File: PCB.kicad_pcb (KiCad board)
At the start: 4 copper layers, 130.2 x 64.3 mm, 31 parts, among them J1 Conn_ARM_SWD_TagConnect_TC2030, U2 STM32L476RGTx, U3 NT3H2X11, U4 SSD1306

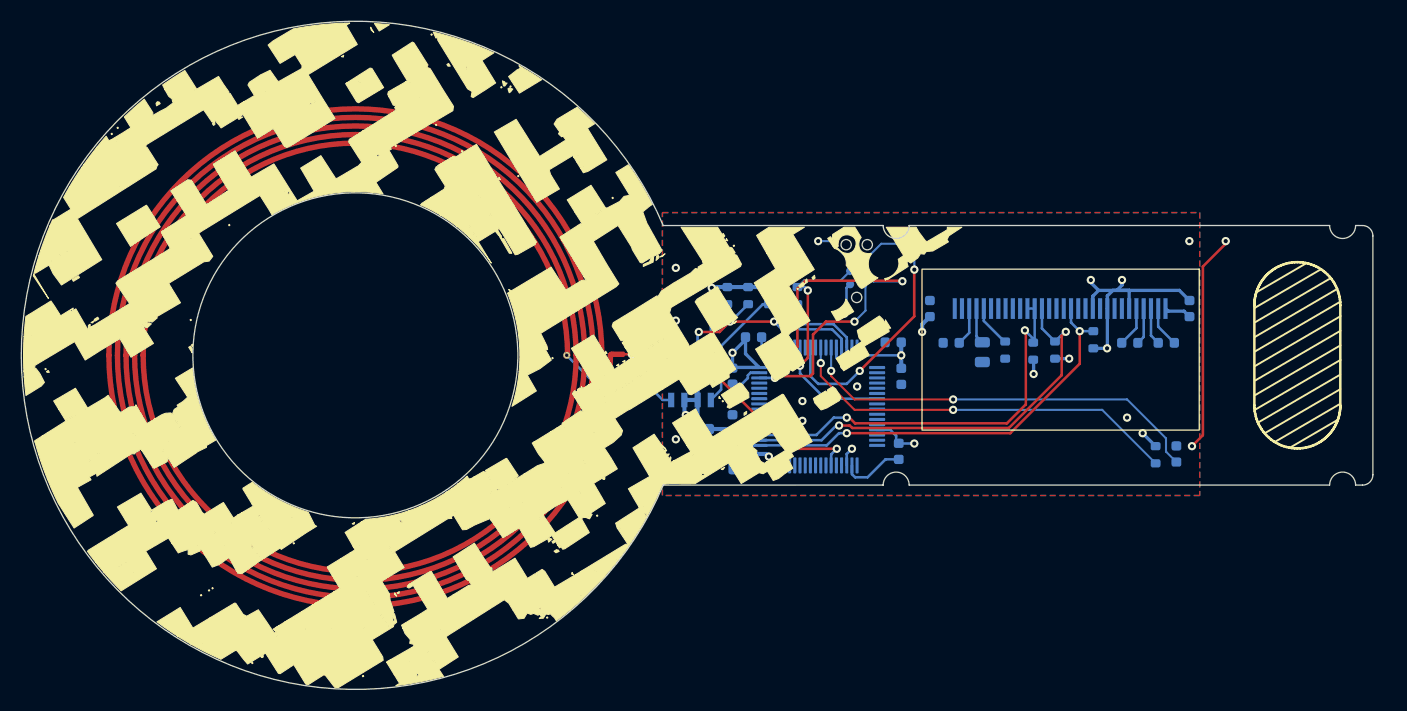
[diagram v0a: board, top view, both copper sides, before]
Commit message: Add board REV-D
Revision D changes the mounting holes so that we can fit screws to
assemble the two case pieces.

Also add required compliance logos on the back.
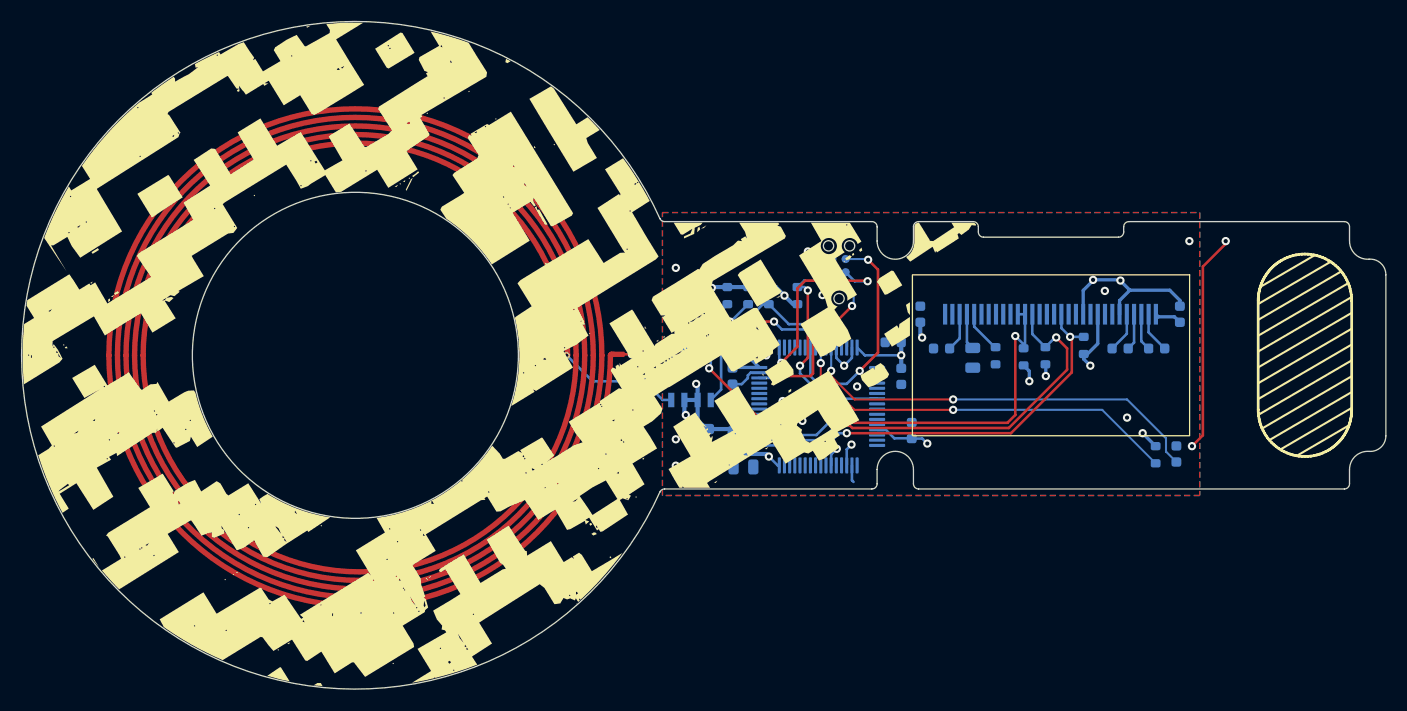
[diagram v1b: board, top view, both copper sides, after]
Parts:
- moved C4 2.36 mm to (136.3, 131.7), turned to 90 degrees
- moved J1 1.70 mm to (129.3, 116.5)
- moved C11 1.07 mm to (142.1, 124.7)
- moved R4 1.07 mm to (152.8, 123.5)
- moved R6 1.07 mm to (149.1, 124.5)
- moved U4 1.07 mm to (149.6, 120.5)
- moved C13 1.07 mm to (159.8, 123.8)
- moved C7 1.07 mm to (139.1, 123.8)
- moved R7 1.07 mm to (147.0, 124.6)
- moved C10 1.07 mm to (162.1, 120.5)
- moved C17 1.07 mm to (137.1, 120.5)
- moved R5 1.07 mm to (144.3, 124.5)
- moved C12 1.07 mm to (156.3, 123.8)
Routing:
- net GND: track 46.4 -> 40.8 mm, vias 17 -> 18
- net SWO: track 27.5 -> 22.3 mm
- net SWCLK: track 24.0 -> 18.9 mm
- net VCC: track 82.3 -> 79.9 mm
- net NRST: track 23.6 -> 21.8 mm
- net SWDIO: track 17.7 -> 16.4 mm
- net DISP_SDA: track 40.1 -> 39.0 mm
- net DISP_RES: track 41.1 -> 40.3 mm
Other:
- board size 130.2 x 64.3 mm -> 131.4 x 64.3 mm
- board text added: "Board Rev 2D 04/20/2024"
- board text removed: "Board Rev 2C 01/25/2024"
